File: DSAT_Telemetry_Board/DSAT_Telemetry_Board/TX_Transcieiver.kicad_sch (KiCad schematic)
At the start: 15 parts

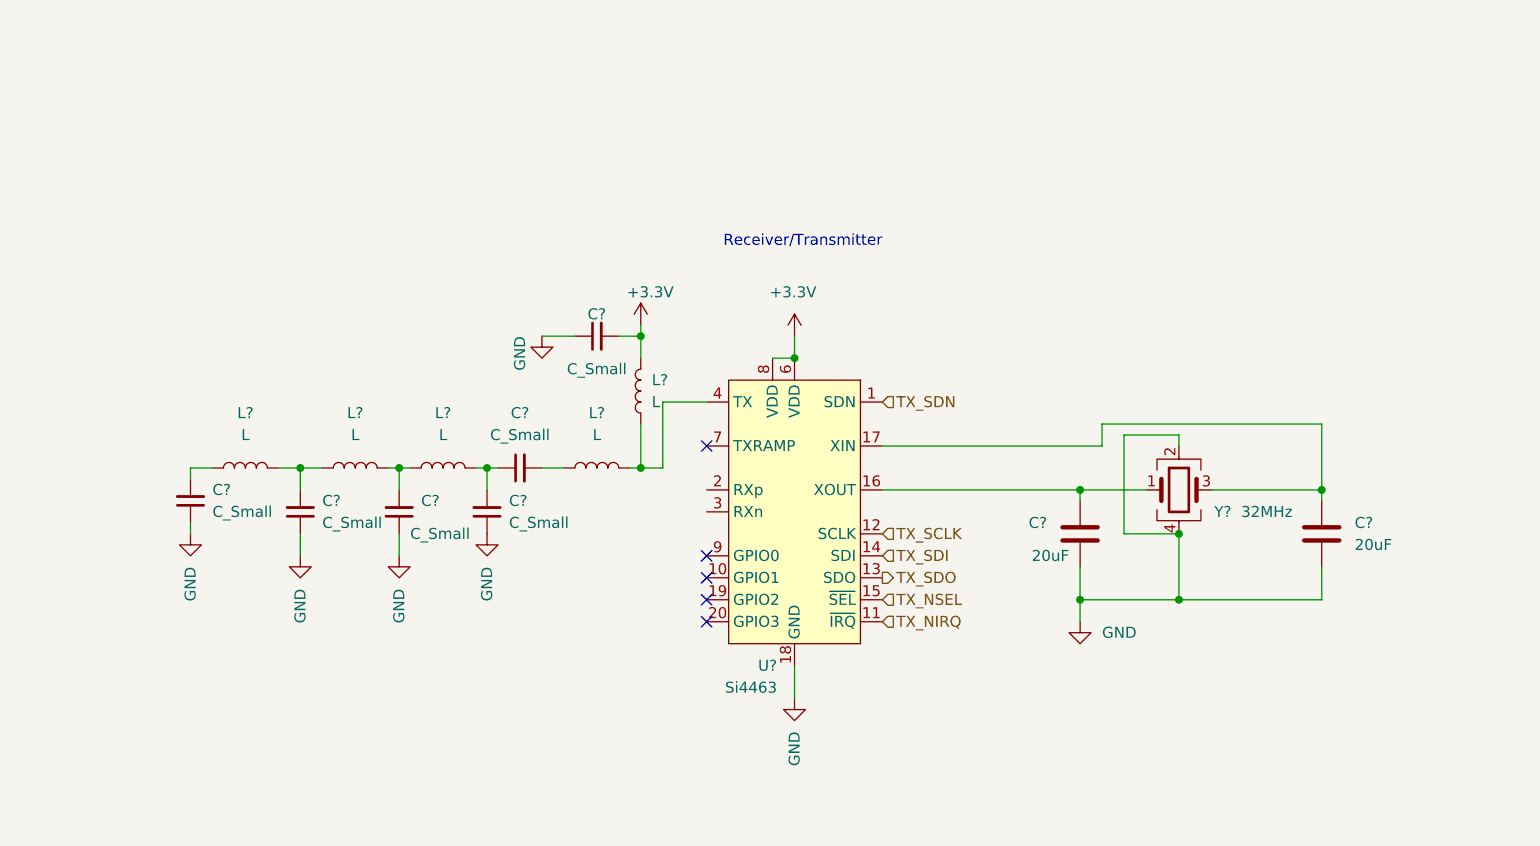
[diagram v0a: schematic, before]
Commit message: RX_SWitch, test points
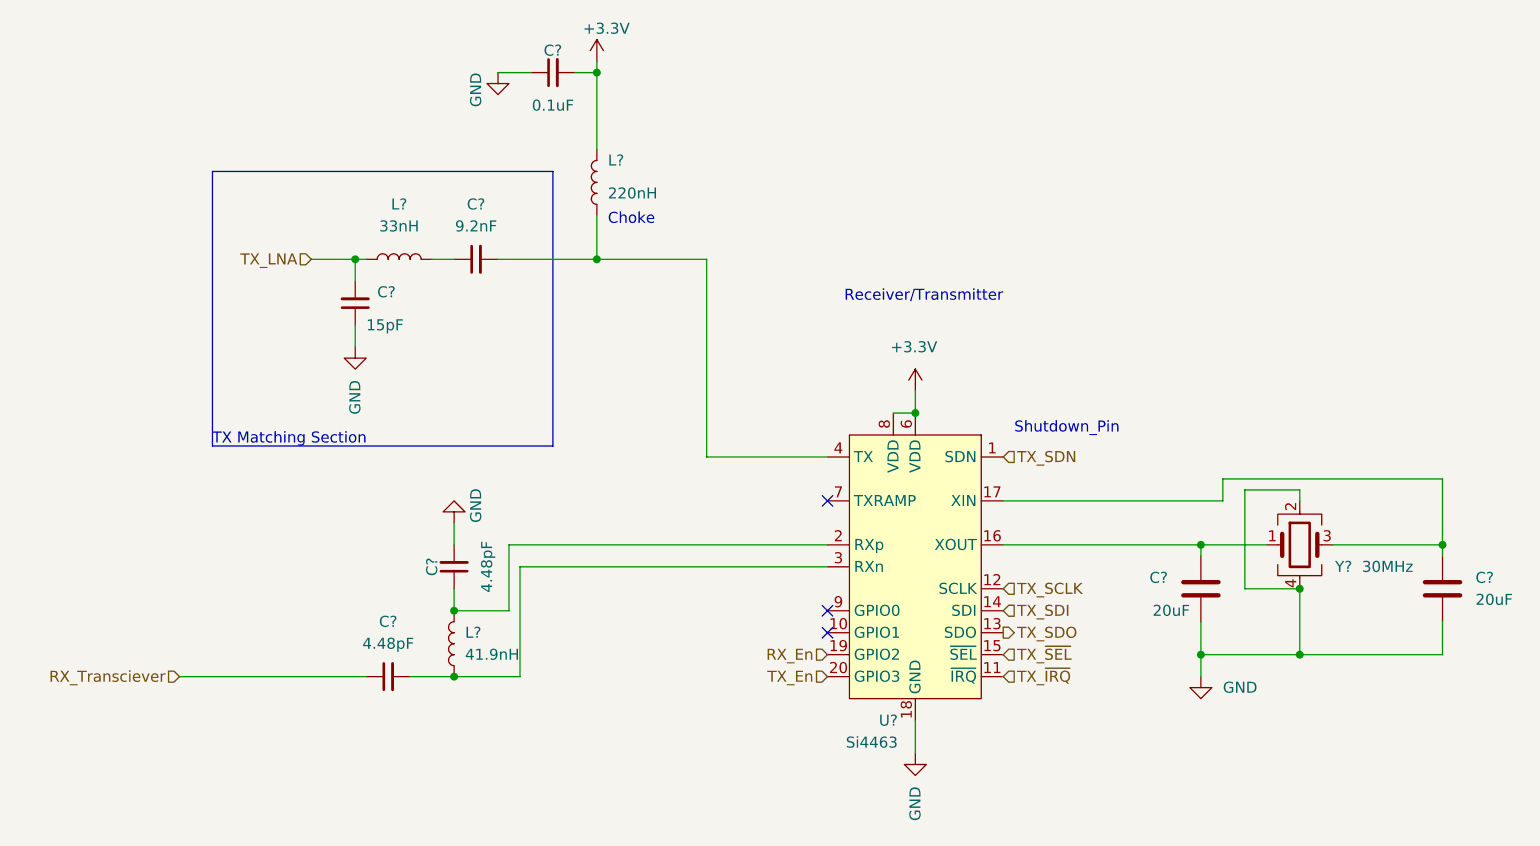
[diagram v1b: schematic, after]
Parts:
- removed C? (x5): C_Small, Capacitor_SMD:C_0201_0603Metric, symbol Device:C_Small
- removed C? (x2): 20uF, Capacitor_SMD:C_0201_0603Metric, symbol Device:C
- removed C?: C_Small, symbol Device:C_Small
- removed L? (x5): L, symbol Device:L
- removed U?: Si4463, Package_DFN_QFN:QFN-20-1EP_4x4mm_P0.5mm_EP2.6x2.6mm_ThermalVias, symbol RF:Si4463
- removed Y?: 32MHz, symbol Device:Crystal_GND24
- added C?: 15pF, Capacitor_SMD:C_0402_1005Metric_Pad0.74x0.62mm_HandSolder, symbol Device:C_Small
- added C? (x2): 20uF, Capacitor_SMD:C_0402_1005Metric_Pad0.74x0.62mm_HandSolder, symbol Device:C
- added C? (x2): 4.48pF, Capacitor_SMD:C_0402_1005Metric_Pad0.74x0.62mm_HandSolder, symbol Device:C_Small
- added C?: 0.1uF, Capacitor_SMD:C_0402_1005Metric_Pad0.74x0.62mm_HandSolder, symbol Device:C_Small
- added C?: 9.2nF, Capacitor_SMD:C_0402_1005Metric_Pad0.74x0.62mm_HandSolder, symbol Device:C_Small
- added L?: 220nH, Inductor_SMD:L_0402_1005Metric_Pad0.77x0.64mm_HandSolder, symbol Device:L
- added L?: 33nH, Inductor_SMD:L_0402_1005Metric_Pad0.77x0.64mm_HandSolder, symbol Device:L
- added L?: 41.9nH, Inductor_SMD:L_0402_1005Metric_Pad0.77x0.64mm_HandSolder, symbol Device:L
- added U?: Si4463, Package_DFN_QFN:QFN-20-1EP_4x4mm_P0.5mm_EP2.6x2.6mm_ThermalVias, symbol RF:Si4463
- added Y?: 30MHz, symbol Device:Crystal_GND24
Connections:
- net +3.3V: now also C?.2, L?.2, U?.6 (VDD), U?.8 (VDD)
- net GND: now also C?.1, C?.1, C?.1, C?.2, C?.2, U?.18 (GND), U?.21 (GND), Y?.2, Y?.4
- net TX_SCLK: now also U?.12 (SCLK)
- net TX_SDI: now also U?.14 (SDI)
- net TX_SDN: now also U?.1 (SDN)
- net TX_SDO: now also U?.13 (SDO)
- new net: C?.2, U?.16 (XOUT), Y?.1
- new net: C?.1, U?.17 (XIN), Y?.3
- new net: C?.1, L?.2, U?.2 (RXp)
- new net: C?.2, L?.1, U?.3 (RXn)
- new net: C?.2, L?.1, U?.4 (TX)
- new net: C?.1, L?.2
- new net RX_En: U?.19 (GPIO2)
- new net RX_Transciever: C?.1
- new net TX_En: U?.20 (GPIO3)
- new net TX_LNA: C?.2, L?.1
- new net TX_~{IRQ}: U?.11 (~{IRQ})
- new net TX_~{SEL}: U?.15 (~{SEL})
- no-connect marks 5 -> 3
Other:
- note added: "Choke"
- note added: "Shutdown_Pin"
- note added: "TX Matching Section"

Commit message: RX_SWitch, test points
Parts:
- Y2: renamed from Y?; footprint (none) -> Crystal:Crystal_SMD_2520-4Pin_2.5x2.0mm
- gave numbers to parts that had none: 11
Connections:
- net at L3.1, U6.4 (TX): now also C23.1; no longer C23.2
- net TX_Transceiver: now reaches L1.2
- net TX_Transceiver: now also C20.2; no longer C23.1
- net TX_LNA: no longer names the net of L1.1
- net TX_LNA: now also C23.2; no longer C20.2
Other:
- moved on the sheet: C23, L1
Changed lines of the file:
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@@
     (effects (font (size 1.27 1.27)) (justify left bottom))
   )
-  (hierarchical_label "TX_LNA" (shape input) (at 68.58 69.85 180)
+  (hierarchical_label "TX_Transceiver" (shape input) (at 68.58 69.85 180)
     (effects (font (size 1.27 1.27)) (justify right))
   )
@@
     (effects (font (size 1.27 1.27)) (justify left))
   )
-  (symbol (lib_id "Device:C_Small") (at 73.66 74.93 180)
-    (in_bom yes) (on_board yes)
-    (property "Reference" "C?" (id 0) (at 76.2 73.6535 0)
+  (symbol (lib_id "Device:C_Small") (at 73.66 74.93 180) (unit 1)
+    (in_bom yes) (on_board yes)
+    (property "Reference" "C20" (id 0) (at 76.2 73.6535 0)
       (effects (font (size 1.27 1.27)) (justify right))
     )
@@
     (pin "2")
   )
-  (symbol (lib_id "RF:Si4463") (at 138.43 105.41 0) (mirror y)
-    (in_bom yes) (on_board yes) (fields_autoplaced)
-    (property "Reference" "U?" (id 0) (at 136.4106 123.19 0)
+  (symbol (lib_id "RF:Si4463") (at 138.43 105.41 0) (mirror y) (unit 1)
+    (in_bom yes) (on_board yes) (fields_autoplaced)
+    (property "Reference" "U6" (id 0) (at 136.4106 123.19 0)
       (effects (font (size 1.27 1.27)) (justify left))
     )
@@
     (pin "9")
   )
-  (symbol (lib_id "power:+3.3V") (at 101.6 46.99 0)
-    (in_bom yes) (on_board yes)
-    (property "Reference" "#PWR?" (id 0) (at 101.6 50.8 0)
+  (symbol (lib_id "power:+3.3V") (at 101.6 46.99 0) (unit 1)
+    (in_bom yes) (on_board yes)
+    (property "Reference" "#PWR0134" (id 0) (at 101.6 50.8 0)
       (effects (font (size 1.27 1.27)) hide)
     )
@@
     (pin "1")
   )
-  (symbol (lib_id "Device:C") (at 171.45 107.95 0) (mirror x)
-    (in_bom yes) (on_board yes)
-    (property "Reference" "C?" (id 0) (at 167.64 106.6799 0)
+  (symbol (lib_id "Device:C") (at 171.45 107.95 0) (mirror x) (unit 1)
+    (in_bom yes) (on_board yes)
+    (property "Reference" "C25" (id 0) (at 167.64 106.6799 0)
       (effects (font (size 1.27 1.27)) (justify right))
     )
@@
     (pin "2")
   )
-  (symbol (lib_id "Device:Crystal_GND24") (at 182.88 102.87 0)
-    (in_bom yes) (on_board yes)
-    (property "Reference" "Y?" (id 0) (at 187.96 105.41 0))
+  (symbol (lib_id "Device:Crystal_GND24") (at 182.88 102.87 0) (unit 1)
+    (in_bom yes) (on_board yes)
+    (property "Reference" "Y2" (id 0) (at 187.96 105.41 0))
     (property "Value" "30MHz" (id 1) (at 193.04 105.41 0))
-    (property "Footprint" "" (id 2) (at 182.88 102.87 0)
+    (property "Footprint" "Crystal:Crystal_SMD_2520-4Pin_2.5x2.0mm" (id 2) (at 182.88 102.87 0)
       (effects (font (size 1.27 1.27)) hide)
     )
@@
     (pin "4")
   )
-  (symbol (lib_id "power:GND") (at 73.66 80.01 0) (mirror y)
-    (in_bom yes) (on_board yes) (fields_autoplaced)
-    (property "Reference" "#PWR?" (id 0) (at 73.66 86.36 0)
+  (symbol (lib_id "power:GND") (at 73.66 80.01 0) (mirror y) (unit 1)
+    (in_bom yes) (on_board yes) (fields_autoplaced)
+    (property "Reference" "#PWR0137" (id 0) (at 73.66 86.36 0)
       (effects (font (size 1.27 1.27)) hide)
     )
@@
     (pin "1")
   )
-  (symbol (lib_id "power:GND") (at 138.43 127 0) (mirror y)
-    (in_bom yes) (on_board yes) (fields_autoplaced)
-    (property "Reference" "#PWR?" (id 0) (at 138.43 133.35 0)
+  (symbol (lib_id "power:GND") (at 138.43 127 0) (mirror y) (unit 1)
+    (in_bom yes) (on_board yes) (fields_autoplaced)
+    (property "Reference" "#PWR0139" (id 0) (at 138.43 133.35 0)
       (effects (font (size 1.27 1.27)) hide)
     )
@@
     (pin "1")
   )
-  (symbol (lib_id "power:GND") (at 85.09 100.33 0) (mirror x)
-    (in_bom yes) (on_board yes)
-    (property "Reference" "#PWR?" (id 0) (at 85.09 93.98 0)
+  (symbol (lib_id "power:GND") (at 85.09 100.33 0) (mirror x) (unit 1)
+    (in_bom yes) (on_board yes)
+    (property "Reference" "#PWR0136" (id 0) (at 85.09 93.98 0)
       (effects (font (size 1.27 1.27)) hide)
     )
@@
     (pin "1")
   )
-  (symbol (lib_id "Device:C_Small") (at 77.47 118.11 90)
-    (in_bom yes) (on_board yes) (fields_autoplaced)
-    (property "Reference" "C?" (id 0) (at 77.4763 111.76 90))
+  (symbol (lib_id "Device:C_Small") (at 77.47 118.11 90) (unit 1)
+    (in_bom yes) (on_board yes) (fields_autoplaced)
+    (property "Reference" "C21" (id 0) (at 77.4763 111.76 90))
     (property "Value" "4.48pF" (id 1) (at 77.4763 114.3 90))
     (property "Footprint" "Capacitor_SMD:C_0402_1005Metric_Pad0.74x0.62mm_HandSolder" (id 2) (at 77.47 118.11 0)
@@
     (pin "2")
   )
-  (symbol (lib_id "power:GND") (at 171.45 118.11 0)
-    (in_bom yes) (on_board yes)
-    (property "Reference" "#PWR?" (id 0) (at 171.45 124.46 0)
+  (symbol (lib_id "power:GND") (at 171.45 118.11 0) (unit 1)
+    (in_bom yes) (on_board yes)
+    (property "Reference" "#PWR0133" (id 0) (at 171.45 124.46 0)
       (effects (font (size 1.27 1.27)) hide)
     )
@@
     (pin "1")
   )
-  (symbol (lib_id "Device:C_Small") (at 96.52 48.26 90)
-    (in_bom yes) (on_board yes)
-    (property "Reference" "C?" (id 0) (at 96.52 45.72 90))
+  (symbol (lib_id "Device:C_Small") (at 96.52 48.26 90) (unit 1)
+    (in_bom yes) (on_board yes)
+    (property "Reference" "C24" (id 0) (at 96.52 45.72 90))
     (property "Value" "0.1uF" (id 1) (at 96.52 52.07 90))
     (property "Footprint" "Capacitor_SMD:C_0402_1005Metric_Pad0.74x0.62mm_HandSolder" (id 2) (at 96.52 48.26 0)
@@
     (pin "2")
   )
-  (symbol (lib_id "power:GND") (at 90.17 48.26 0) (mirror y)
-    (in_bom yes) (on_board yes)
-    (property "Reference" "#PWR?" (id 0) (at 90.17 54.61 0)
+  (symbol (lib_id "power:GND") (at 90.17 48.26 0) (mirror y) (unit 1)
+    (in_bom yes) (on_board yes)
+    (property "Reference" "#PWR0135" (id 0) (at 90.17 54.61 0)
       (effects (font (size 1.27 1.27)) hide)
     )
@@
     (pin "1")
   )
-  (symbol (lib_id "Device:L") (at 101.6 60.96 180)
-    (in_bom yes) (on_board yes)
-    (property "Reference" "L?" (id 0) (at 102.87 58.42 0)
+  (symbol (lib_id "Device:L") (at 101.6 60.96 180) (unit 1)
+    (in_bom yes) (on_board yes)
+    (property "Reference" "L3" (id 0) (at 102.87 58.42 0)
       (effects (font (size 1.27 1.27)) (justify right))
     )
@@
     (pin "2")
   )
-  (symbol (lib_id "Device:L") (at 78.74 69.85 90)
-    (in_bom yes) (on_board yes) (fields_autoplaced)
-    (property "Reference" "L?" (id 0) (at 78.74 63.5 90))
+  (symbol (lib_id "Device:L") (at 78.74 69.85 270) (mirror x) (unit 1)
+    (in_bom yes) (on_board yes) (fields_autoplaced)
+    (property "Reference" "L1" (id 0) (at 78.74 63.5 90))
     (property "Value" "33nH" (id 1) (at 78.74 66.04 90))
     (property "Footprint" "Inductor_SMD:L_0402_1005Metric_Pad0.77x0.64mm_HandSolder" (id 2) (at 78.74 69.85 0)
@@
     (pin "2")
   )
-  (symbol (lib_id "power:+3.3V") (at 138.43 85.09 0)
-    (in_bom yes) (on_board yes)
-    (property "Reference" "#PWR?" (id 0) (at 138.43 88.9 0)
+  (symbol (lib_id "power:+3.3V") (at 138.43 85.09 0) (unit 1)
+    (in_bom yes) (on_board yes)
+    (property "Reference" "#PWR0138" (id 0) (at 138.43 88.9 0)
       (effects (font (size 1.27 1.27)) hide)
     )
@@
     (pin "1")
   )
-  (symbol (lib_id "Device:C_Small") (at 85.09 105.41 180)
-    (in_bom yes) (on_board yes)
-    (property "Reference" "C?" (id 0) (at 82.55 105.41 90))
+  (symbol (lib_id "Device:C_Small") (at 85.09 105.41 180) (unit 1)
+    (in_bom yes) (on_board yes)
+    (property "Reference" "C22" (id 0) (at 82.55 105.41 90))
     (property "Value" "4.48pF" (id 1) (at 88.9 105.41 90))
     (property "Footprint" "Capacitor_SMD:C_0402_1005Metric_Pad0.74x0.62mm_HandSolder" (id 2) (at 85.09 105.41 0)
@@
     (pin "2")
   )
-  (symbol (lib_id "Device:C") (at 199.39 107.95 0)
-    (in_bom yes) (on_board yes) (fields_autoplaced)
-    (property "Reference" "C?" (id 0) (at 203.2 106.6799 0)
+  (symbol (lib_id "Device:C") (at 199.39 107.95 0) (unit 1)
+    (in_bom yes) (on_board yes) (fields_autoplaced)
+    (property "Reference" "C26" (id 0) (at 203.2 106.6799 0)
       (effects (font (size 1.27 1.27)) (justify left))
     )
@@
     (pin "2")
   )
-  (symbol (lib_id "Device:C_Small") (at 87.63 69.85 90)
-    (in_bom yes) (on_board yes) (fields_autoplaced)
-    (property "Reference" "C?" (id 0) (at 87.6363 63.5 90))
-    (property "Value" "9.2nF" (id 1) (at 87.6363 66.04 90))
+  (symbol (lib_id "Device:C_Small") (at 87.63 69.85 270) (mirror x) (unit 1)
+    (in_bom yes) (on_board yes) (fields_autoplaced)
+    (property "Reference" "C23" (id 0) (at 87.6236 63.5 90))
+    (property "Value" "9.2nF" (id 1) (at 87.6236 66.04 90))
     (property "Footprint" "Capacitor_SMD:C_0402_1005Metric_Pad0.74x0.62mm_HandSolder" (id 2) (at 87.63 69.85 0)
       (effects (font (size 1.27 1.27)) hide)
@@
     (pin "2")
   )
-  (symbol (lib_id "Device:L") (at 85.09 114.3 180)
-    (in_bom yes) (on_board yes) (fields_autoplaced)
-    (property "Reference" "L?" (id 0) (at 86.36 113.0299 0)
-      (effects (font (size 1.27 1.27)) (justify right))
-    )
+  (symbol (lib_id "Device:L") (at 85.09 114.3 180) (unit 1)
+    (in_bom yes) (on_board yes) (fields_autoplaced)
+    (property "Reference" "L2" (id 0) (at 86.36 113.0299 0)
+      (effects (font (size 1.27 1.27)) (justify right))
+    )

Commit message: Layout changes
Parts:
- added C34, C35: 100nF, Capacitor_SMD:C_0402_1005Metric_Pad0.74x0.62mm_HandSolder, symbol Device:C
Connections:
- net +3.3V: now also C34.2, C35.2
- net GND: now also C34.1, C35.1
